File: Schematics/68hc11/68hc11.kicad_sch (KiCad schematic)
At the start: 52 parts, among them J1 USB3076-30-A, J2 DB9_Female, J3 Conn_01x10_Male, J4 Conn_01x10_Male, J5 Conn_01x10_Male, J6 Conn_01x10_Male, J7 Conn_01x10_Male, SW1 Reset, U1 MC68HC11A1CC-PLLC, U10 MCP100-270D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

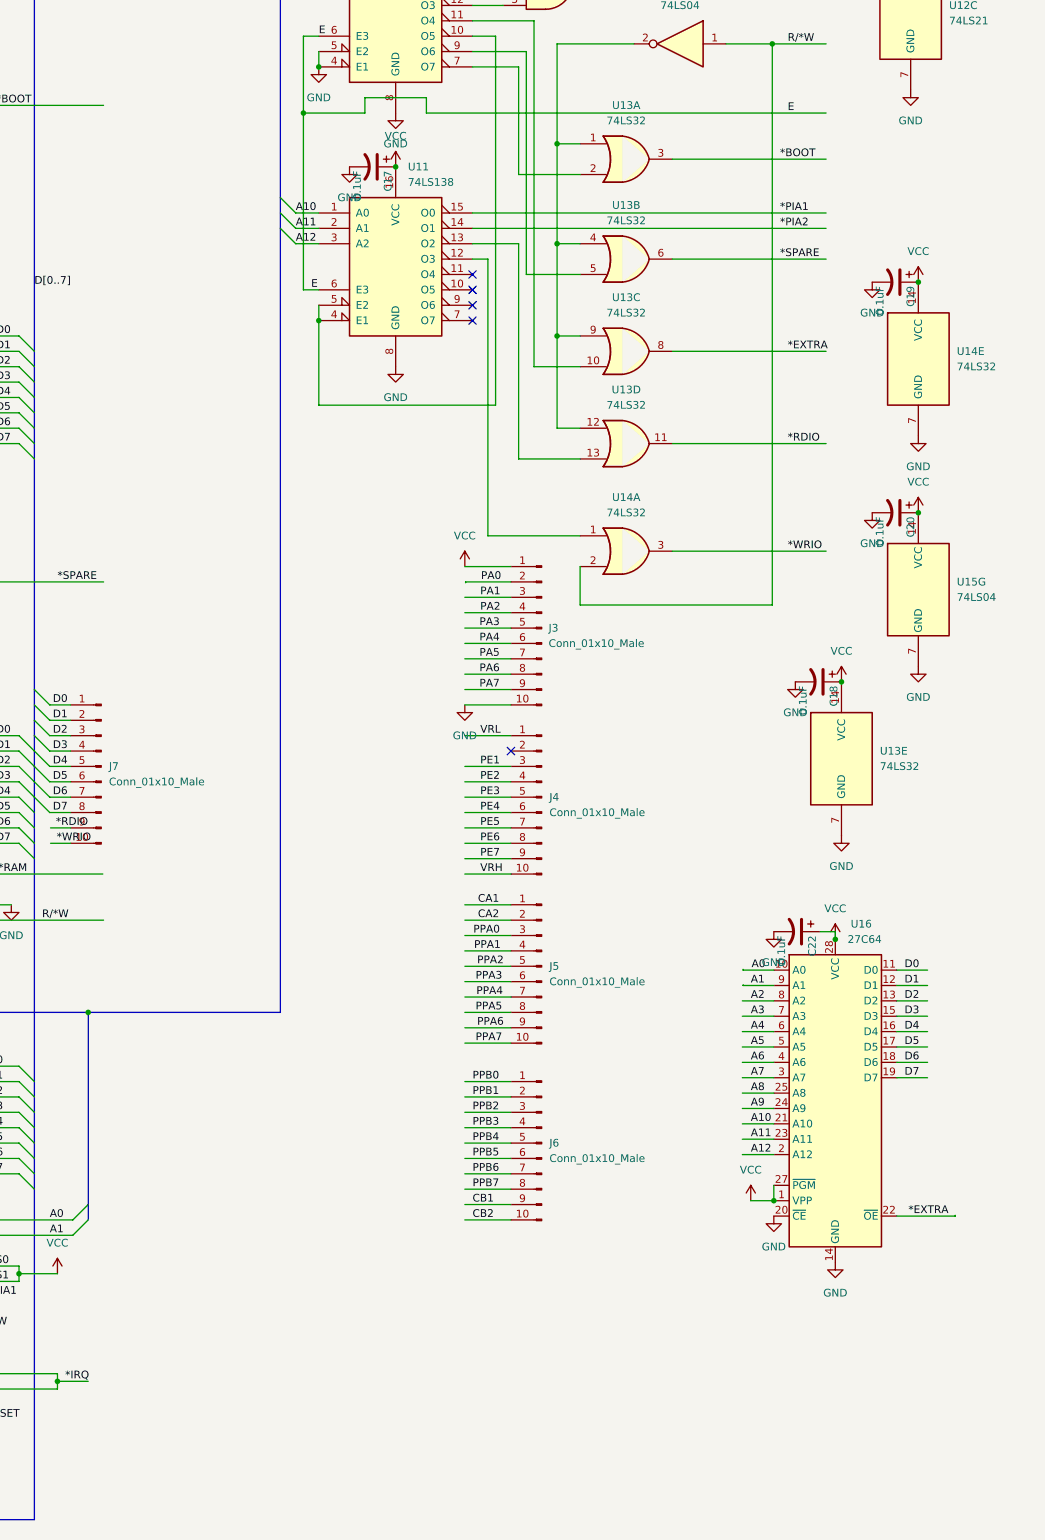
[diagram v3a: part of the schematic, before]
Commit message: Added second PIO chip socket
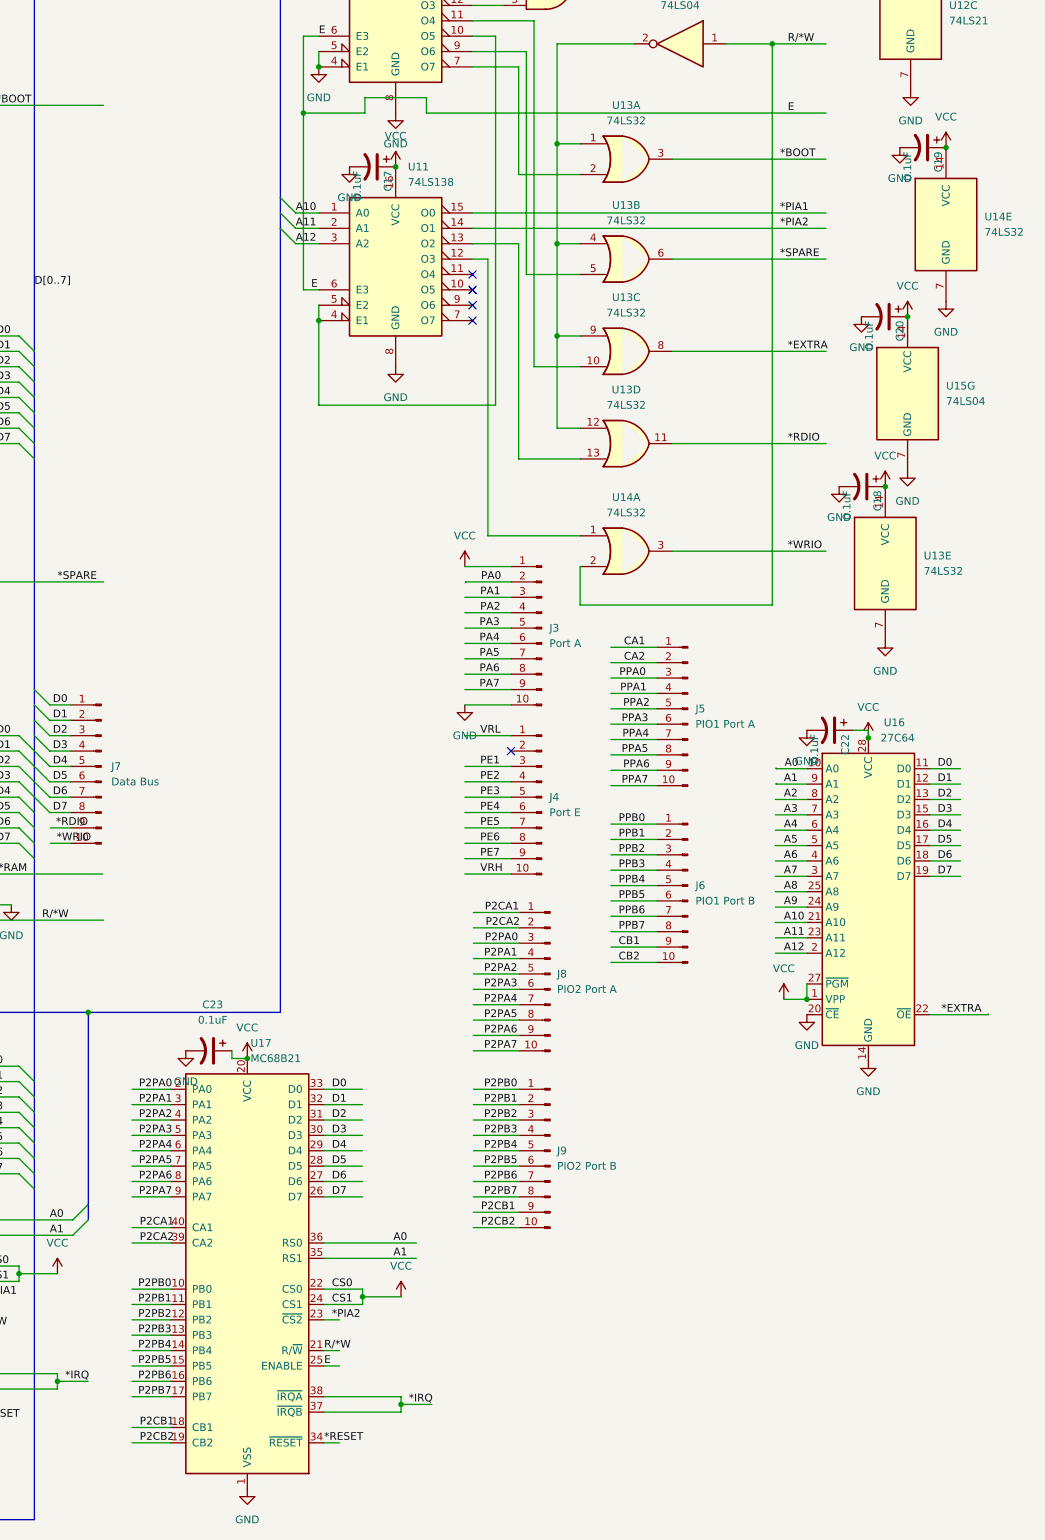
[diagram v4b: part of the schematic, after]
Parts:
- added C23: 0.1uF, Capacitor_THT:C_Disc_D3.0mm_W2.0mm_P2.50mm, symbol Device:C_Polarized_US
- added J8: PIO2 Port A, Connector_PinSocket_2.54mm:PinSocket_1x10_P2.54mm_Vertical, symbol Connector:Conn_01x10_Male
- added J9: PIO2 Port B, Connector_PinSocket_2.54mm:PinSocket_1x10_P2.54mm_Vertical, symbol Connector:Conn_01x10_Male
- added U17: MC68B21, Package_DIP:DIP-40_W15.24mm, symbol Interface:MC68B21
- J3: value Conn_01x10_Male -> Port A
- J4: value Conn_01x10_Male -> Port E
- J5: value Conn_01x10_Male -> PIO1 Port A
- J6: value Conn_01x10_Male -> PIO1 Port B
- J7: value Conn_01x10_Male -> Data Bus
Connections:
- net *IRQ: now also U17.37 (~{IRQB}), U17.38 (~{IRQA})
- net *PIA2: now also U17.23 (~{CS2})
- net *RESET: now also U17.34 (~{RESET})
- net A0: now also U17.36 (RS0)
- net A1: now also U17.35 (RS1)
- net D0: now also U17.33 (D0)
- net D1: now also U17.32 (D1)
- net D2: now also U17.31 (D2)
- net D3: now also U17.30 (D3)
- net D4: now also U17.29 (D4)
- net D5: now also U17.28 (D5)
- net D6: now also U17.27 (D6)
- net D7: now also U17.26 (D7)
- net E: now also U17.25 (ENABLE)
- net GND: now also C23.2, U17.1 (VSS)
- net R/*W: now also U17.21 (R/~{W})
- net VCC: now also C23.1, U17.20 (VCC), U17.22 (CS0), U17.24 (CS1)
- new net P2CA1: J8.1 (Pin_1), U17.40 (CA1)
- new net P2CA2: J8.2 (Pin_2), U17.39 (CA2)
- new net P2CB1: J9.9 (Pin_9), U17.18 (CB1)
- new net P2CB2: J9.10 (Pin_10), U17.19 (CB2)
- new net P2PA0: J8.3 (Pin_3), U17.2 (PA0)
- new net P2PA1: J8.4 (Pin_4), U17.3 (PA1)
- new net P2PA2: J8.5 (Pin_5), U17.4 (PA2)
- new net P2PA3: J8.6 (Pin_6), U17.5 (PA3)
- new net P2PA4: J8.7 (Pin_7), U17.6 (PA4)
- new net P2PA5: J8.8 (Pin_8), U17.7 (PA5)
- new net P2PA6: J8.9 (Pin_9), U17.8 (PA6)
- new net P2PA7: J8.10 (Pin_10), U17.9 (PA7)
- new net P2PB0: J9.1 (Pin_1), U17.10 (PB0)
- new net P2PB1: J9.2 (Pin_2), U17.11 (PB1)
- new net P2PB2: J9.3 (Pin_3), U17.12 (PB2)
- new net P2PB3: J9.4 (Pin_4), U17.13 (PB3)
- new net P2PB4: J9.5 (Pin_5), U17.14 (PB4)
- new net P2PB5: J9.6 (Pin_6), U17.15 (PB5)
- new net P2PB6: J9.7 (Pin_7), U17.16 (PB6)
- new net P2PB7: J9.8 (Pin_8), U17.17 (PB7)
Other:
- moved on the sheet: C18, C19, C20, C22, J5, J6, U13E, U14E, U15G, U16

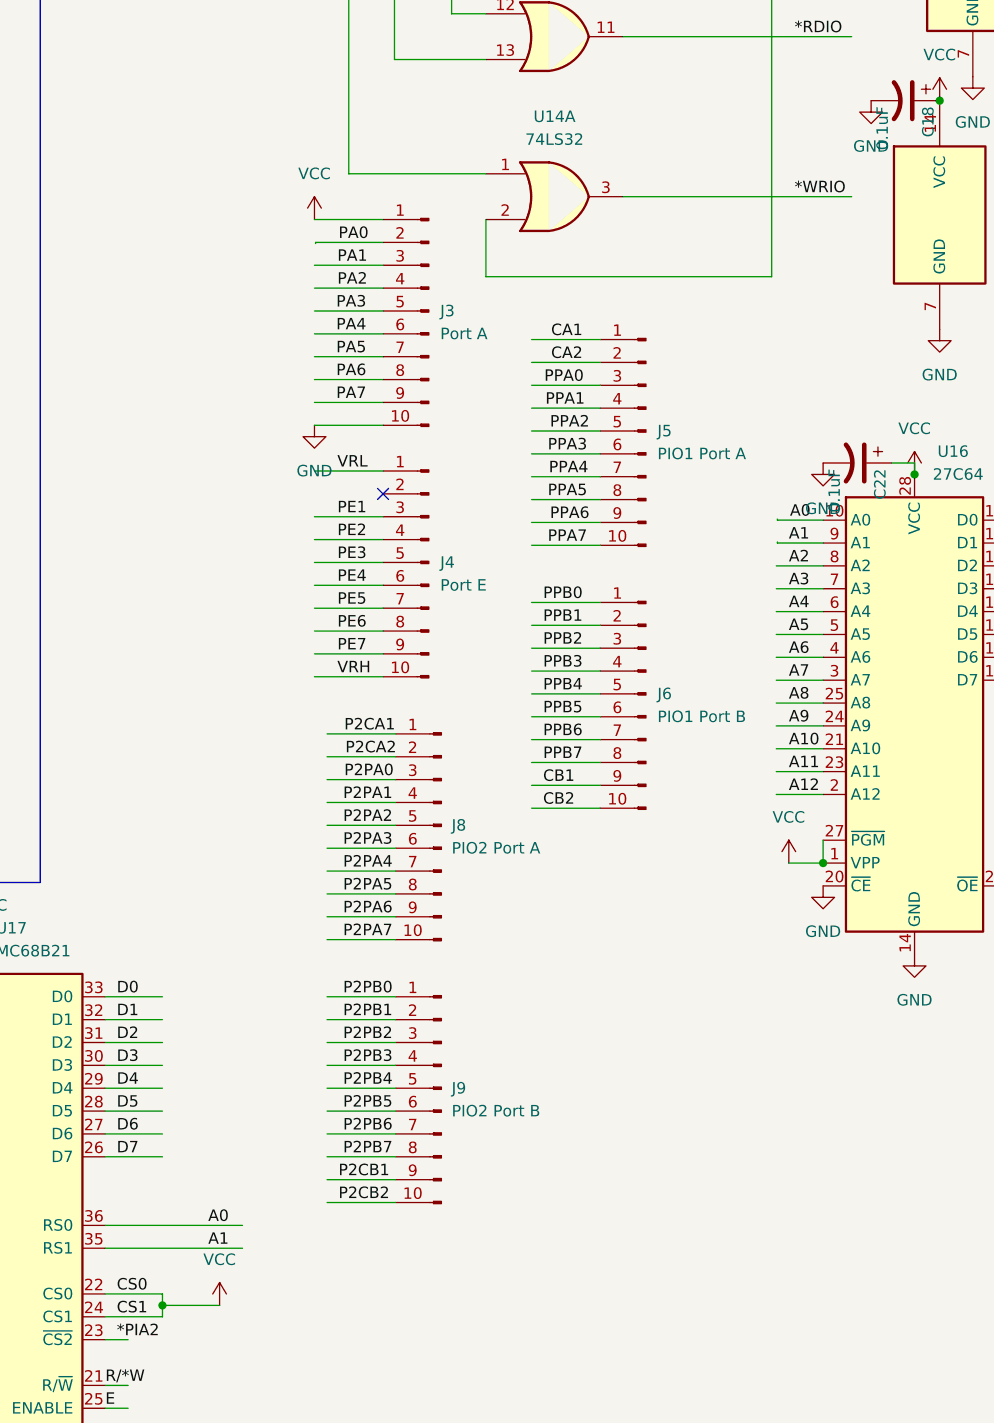
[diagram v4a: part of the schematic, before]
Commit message: Wired Data Bus
Corrected discrepency between pin sockets and footprints turned 2 10 pin into 1 20 socket
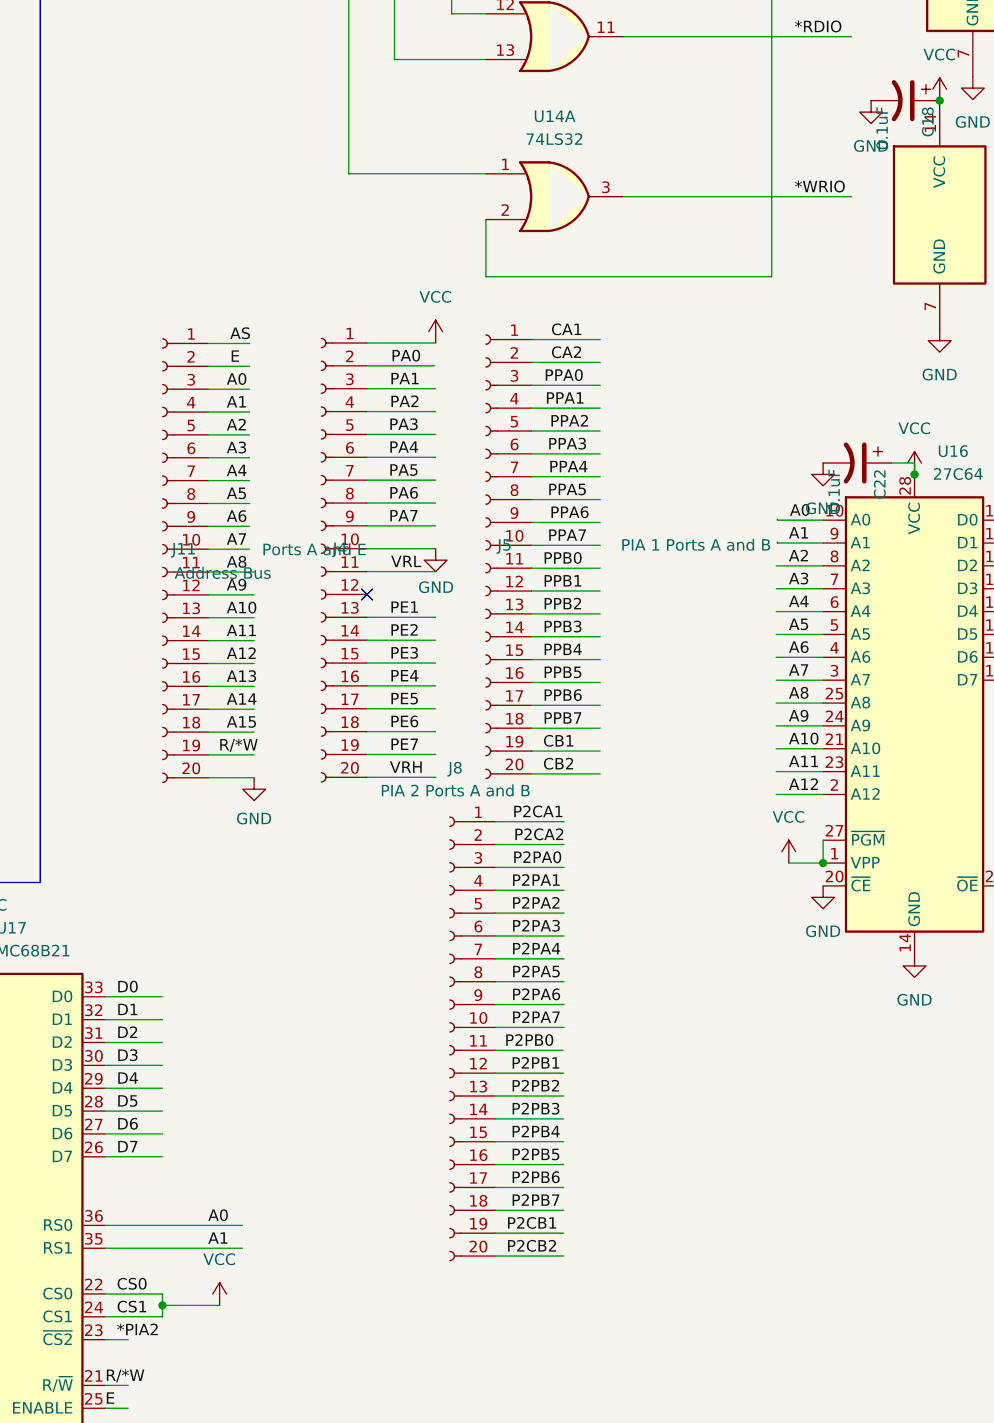
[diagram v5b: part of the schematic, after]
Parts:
- removed J3: Port A, Connector_PinSocket_2.54mm:PinSocket_1x10_P2.54mm_Vertical, symbol Connector:Conn_01x10_Male
- removed J6: PIO1 Port B, Connector_PinSocket_2.54mm:PinSocket_1x10_P2.54mm_Vertical, symbol Connector:Conn_01x10_Male
- removed J9: PIO2 Port B, Connector_PinSocket_2.54mm:PinSocket_1x10_P2.54mm_Vertical, symbol Connector:Conn_01x10_Male
- added J11: Address Bus, Connector_PinSocket_2.54mm:PinSocket_1x20_P2.54mm_Vertical, symbol Connector:Conn_01x20_Female
- J4: value Port E -> Ports A and E; footprint Connector_PinSocket_2.54mm:PinSocket_1x10_P2.54mm_Vertical -> Connector_PinSocket_2.54mm:PinSocket_1x20_P2.54mm_Vertical; symbol Connector:Conn_01x10_Male -> Connector:Conn_01x20_Female
- J5: value PIO1 Port A -> PIA 1 Ports A and B; footprint Connector_PinSocket_2.54mm:PinSocket_1x10_P2.54mm_Vertical -> Connector_PinSocket_2.54mm:PinSocket_1x20_P2.54mm_Vertical; symbol Connector:Conn_01x10_Male -> Connector:Conn_01x20_Female
- J8: value PIO2 Port A -> PIA 2 Ports A and B; footprint Connector_PinSocket_2.54mm:PinSocket_1x10_P2.54mm_Vertical -> Connector_PinSocket_2.54mm:PinSocket_1x20_P2.54mm_Vertical; symbol Connector:Conn_01x10_Male -> Connector:Conn_01x20_Female
- JP4: footprint Connector_PinHeader_1.00mm:PinHeader_1x03_P1.00mm_Vertical -> Connector_PinHeader_2.54mm:PinHeader_1x03_P2.54mm_Vertical
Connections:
- net A0: now also J11.3 (Pin_3)
- net A1: now also J11.4 (Pin_4)
- net A10: now also J11.13 (Pin_13)
- net A11: now also J11.14 (Pin_14)
- net A12: now also J11.15 (Pin_15)
- net A13: now also J11.16 (Pin_16)
- net A14: now also J11.17 (Pin_17)
- net A15: now also J11.18 (Pin_18)
- net A2: now also J11.5 (Pin_5)
- net A3: now also J11.6 (Pin_6)
- net A4: now also J11.7 (Pin_7)
- net A5: now also J11.8 (Pin_8)
- net A6: now also J11.9 (Pin_9)
- net A7: now also J11.10 (Pin_10)
- net A8: now also J11.11 (Pin_11)
- net A9: now also J11.12 (Pin_12)
- net AS: now also J11.1 (Pin_1)
- net CB1: now also J5.19 (Pin_19)
- net CB2: now also J5.20 (Pin_20)
- net E: now also J11.2 (Pin_2)
- net GND: now also J4.10 (Pin_10), J11.20 (Pin_20)
- net P2CB1: now also J8.19 (Pin_19)
- net P2CB2: now also J8.20 (Pin_20)
- net P2PB0: now also J8.11 (Pin_11)
- net P2PB1: now also J8.12 (Pin_12)
- net P2PB2: now also J8.13 (Pin_13)
- net P2PB3: now also J8.14 (Pin_14)
- net P2PB4: now also J8.15 (Pin_15)
- net P2PB5: now also J8.16 (Pin_16)
- net P2PB6: now also J8.17 (Pin_17)
- net P2PB7: now also J8.18 (Pin_18)
- net PA0: now also J4.2 (Pin_2)
- net PA1: now also J4.3 (Pin_3)
- net PA2: now also J4.4 (Pin_4)
- net PA3: now also J4.5 (Pin_5)
- net PA4: now also J4.6 (Pin_6)
- net PA5: now also J4.7 (Pin_7)
- net PA6: now also J4.8 (Pin_8)
- net PA7: now also J4.9 (Pin_9)
- net PE1: now also J4.13 (Pin_13); no longer J4.3 (Pin_3)
- net PE2: now also J4.14 (Pin_14); no longer J4.4 (Pin_4)
- net PE3: now also J4.15 (Pin_15); no longer J4.5 (Pin_5)
- net PE4: now also J4.16 (Pin_16); no longer J4.6 (Pin_6)
- net PE5: now also J4.17 (Pin_17); no longer J4.7 (Pin_7)
- net PE6: now also J4.18 (Pin_18); no longer J4.8 (Pin_8)
- net PE7: now also J4.19 (Pin_19); no longer J4.9 (Pin_9)
- net PPB0: now also J5.11 (Pin_11)
- net PPB1: now also J5.12 (Pin_12)
- net PPB2: now also J5.13 (Pin_13)
- net PPB3: now also J5.14 (Pin_14)
- net PPB4: now also J5.15 (Pin_15)
- net PPB5: now also J5.16 (Pin_16)
- net PPB6: now also J5.17 (Pin_17)
- net PPB7: now also J5.18 (Pin_18)
- net R/*W: now also J11.19 (Pin_19)
- net VCC: now also J4.1 (Pin_1)
- net VRH: now also J4.20 (Pin_20); no longer J4.10 (Pin_10)
- net VRL: now also J4.11 (Pin_11); no longer J4.1 (Pin_1)

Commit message: Reverted symbols to library standard
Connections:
- net GND: now also J1.6 (Shield), J2.0 (PAD); no longer J1.SH (Shield)
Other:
- moved on the sheet: C11, C12, R2, Y1

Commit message: Getting closer
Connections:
- net GND: now also J1.SH (Shield); no longer J1.6 (Shield)
- net *R/W: now reaches U13.1, U13.12, U13.4, U13.9, U15.2
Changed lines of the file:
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@@
     (stroke (width 0) (type default) (color 0 0 0 0))
   )
-  (wire (pts (xy 307.34 58.42) (xy 297.18 58.42))
-    (stroke (width 0) (type default) (color 0 0 0 0))
-  )
   (wire (pts (xy 370.205 171.831) (xy 365.125 171.831))
     (stroke (width 0) (type default) (color 0 0 0 0))
@@
     (stroke (width 0) (type default) (color 0 0 0 0))
   )
-  (wire (pts (xy 373.38 60.96) (xy 307.34 60.96))
-    (stroke (width 0) (type default) (color 0 0 0 0))
-  )
   (wire (pts (xy 319.532 149.606) (xy 327.152 149.606))
     (stroke (width 0) (type default) (color 0 0 0 0))
@@
     (stroke (width 0) (type default) (color 0 0 0 0))
   )
-  (wire (pts (xy 297.18 58.42) (xy 297.18 60.96))
-    (stroke (width 0) (type default) (color 0 0 0 0))
-  )
   (bus (pts (xy 185.42 99.06) (xy 185.42 293.37))
     (stroke (width 0) (type default) (color 0 0 0 0))
@@
     (stroke (width 0) (type default) (color 0 0 0 0))
   )
-  (wire (pts (xy 307.34 60.96) (xy 307.34 58.42))
-    (stroke (width 0) (type default) (color 0 0 0 0))
-  )
   (wire (pts (xy 356.87 49.53) (xy 364.49 49.53))
     (stroke (width 0) (type default) (color 0 0 0 0))
@@
     (stroke (width 0) (type default) (color 0 0 0 0))
   )
-  (wire (pts (xy 287.02 60.96) (xy 297.18 60.96))
+  (wire (pts (xy 276.86 60.96) (xy 287.02 60.96))
     (stroke (width 0) (type default) (color 0 0 0 0))
   )
@@
     (effects (font (size 1.27 1.27)) (justify left bottom))
   )
-  (label "E" (at 367.03 60.96 0)
+  (label "E" (at 279.4 60.96 0)
     (effects (font (size 1.27 1.27)) (justify left bottom))
   )
@@
     (effects (font (size 1.27 1.27)) (justify left bottom))
   )
+  (label "*R{slash}W" (at 333.375 49.53 0)
+    (effects (font (size 1.27 1.27)) (justify left bottom))
+  )
   (label "CB1" (at 203.2 274.32 0)
     (effects (font (size 1.27 1.27)) (justify left bottom))
@@
     (pin "4")
     (pin "5")
-    (pin "6")
+    (pin "SH")
   )
   (symbol (lib_id "Device:C_Polarized_US") (at 383.032 94.615 270) (unit 1)

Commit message: Added PDF of schematic
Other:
- moved on the sheet: C11, C12, C13, C14, C15, C16, C2, C22, C23, C9, J11, J2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
